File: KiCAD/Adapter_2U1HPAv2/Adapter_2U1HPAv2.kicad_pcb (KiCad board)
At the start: 2 copper layers, 5 x 84 mm, 2 parts

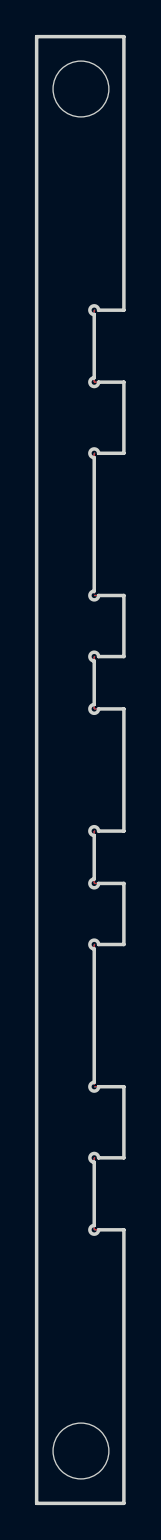
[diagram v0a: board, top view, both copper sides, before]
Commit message: added mechanical solder pads to the adapter boards that were missing them. woops!
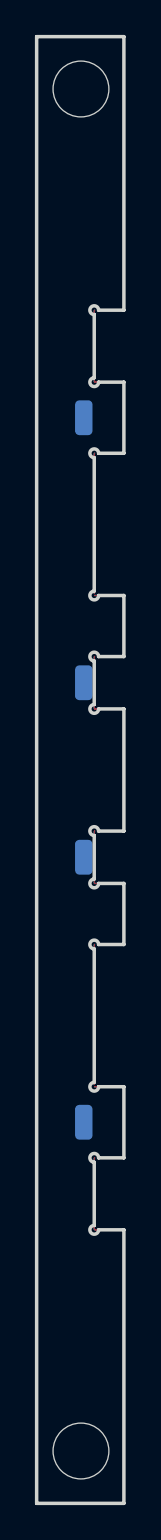
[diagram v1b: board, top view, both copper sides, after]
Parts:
- added MP1: Mechanical_Pad_Solder_Linkage, EXC:SolderWirePad_1x01_SMD_1x2mm, B.Cu at (2.70, 24.3)
- added MP2: Mechanical_Pad_Solder_Linkage, EXC:SolderWirePad_1x01_SMD_1x2mm, B.Cu at (2.70, 39.5)
- added MP3: Mechanical_Pad_Solder_Linkage, EXC:SolderWirePad_1x01_SMD_1x2mm, B.Cu at (2.70, 49.5)
- added MP4: Mechanical_Pad_Solder_Linkage, EXC:SolderWirePad_1x01_SMD_1x2mm, B.Cu at (2.70, 64.6)

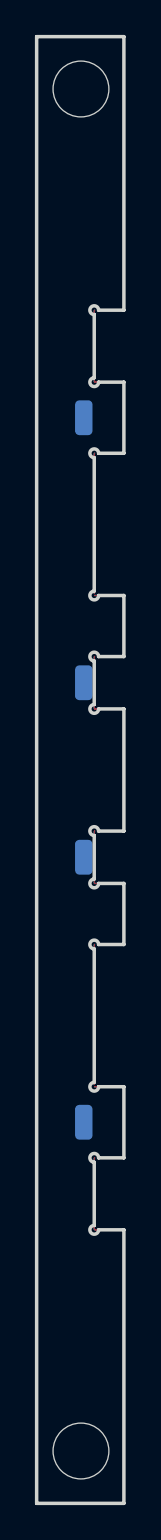
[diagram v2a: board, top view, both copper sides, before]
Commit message: updated all modules to use plated through-holes wherever possible
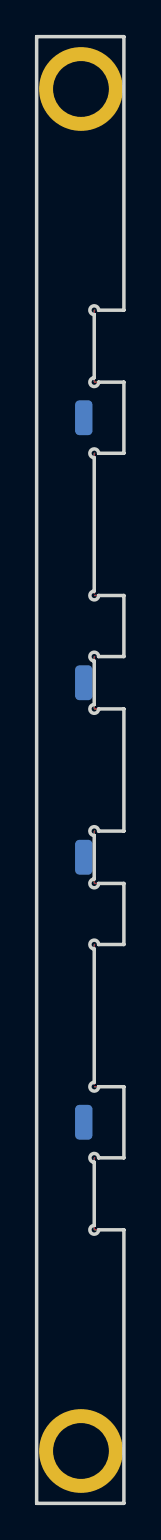
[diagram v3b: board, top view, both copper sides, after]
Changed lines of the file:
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@@
 			)
 		)
-		(pad "" np_thru_hole circle
+		(pad "" thru_hole circle
 			(at 0 0)
-			(size 3.2 3.2)
+			(size 4.8 4.8)
 			(drill 3.2)
 			(layers "*.Cu" "*.Mask")
+			(remove_unused_layers no)
 		)
 		(embedded_fonts no)
@@
 			)
 		)
-		(pad "" np_thru_hole circle
+		(pad "" thru_hole circle
 			(at 0 0)
-			(size 3.2 3.2)
+			(size 4.8 4.8)
 			(drill 3.2)
 			(layers "*.Cu" "*.Mask")
+			(remove_unused_layers no)
 		)
 		(embedded_fonts no)
